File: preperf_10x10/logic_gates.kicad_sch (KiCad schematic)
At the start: 54 parts, among them J10 Conn_01x01_Pin, J11 Conn_01x01_Pin, J12 Conn_01x06_Pin, J13 Conn_01x02_Pin, J14 Conn_01x02_Pin, J15 Conn_01x02_Pin, J16 Conn_01x02_Pin, J17 Conn_01x01_Pin, J18 Conn_01x01_Pin, J19 Conn_01x01_Pin, J2 Conn_01x02_Pin, J20 Conn_01x01_Pin, J21 Conn_01x01_Pin, J22 Conn_01x01_Pin, J23 Conn_01x01_Pin, J24 Conn_01x01_Pin, J25 Conn_01x01_Pin, J26 Conn_01x01_Pin, J27 Conn_01x01_Pin, J28 Conn_01x01_Pin, J29 Conn_01x01_Pin, J3 Conn_01x02_Pin, J30 Conn_01x01_Pin, J31 Conn_01x01_Pin, J32 Conn_01x01_Pin, J33 Conn_01x02_Pin, J34 Conn_01x02_Pin, J35 Conn_01x02_Pin, J36 Conn_01x02_Pin, J5 Conn_01x02_Pin, J7 Conn_01x02_Pin, J8 Conn_01x01_Pin, J9 Conn_01x01_Pin, SW1 SW_DIP_x06, U1 74LS08, U3 74LS32, U4 74LS04, U5 74LS386

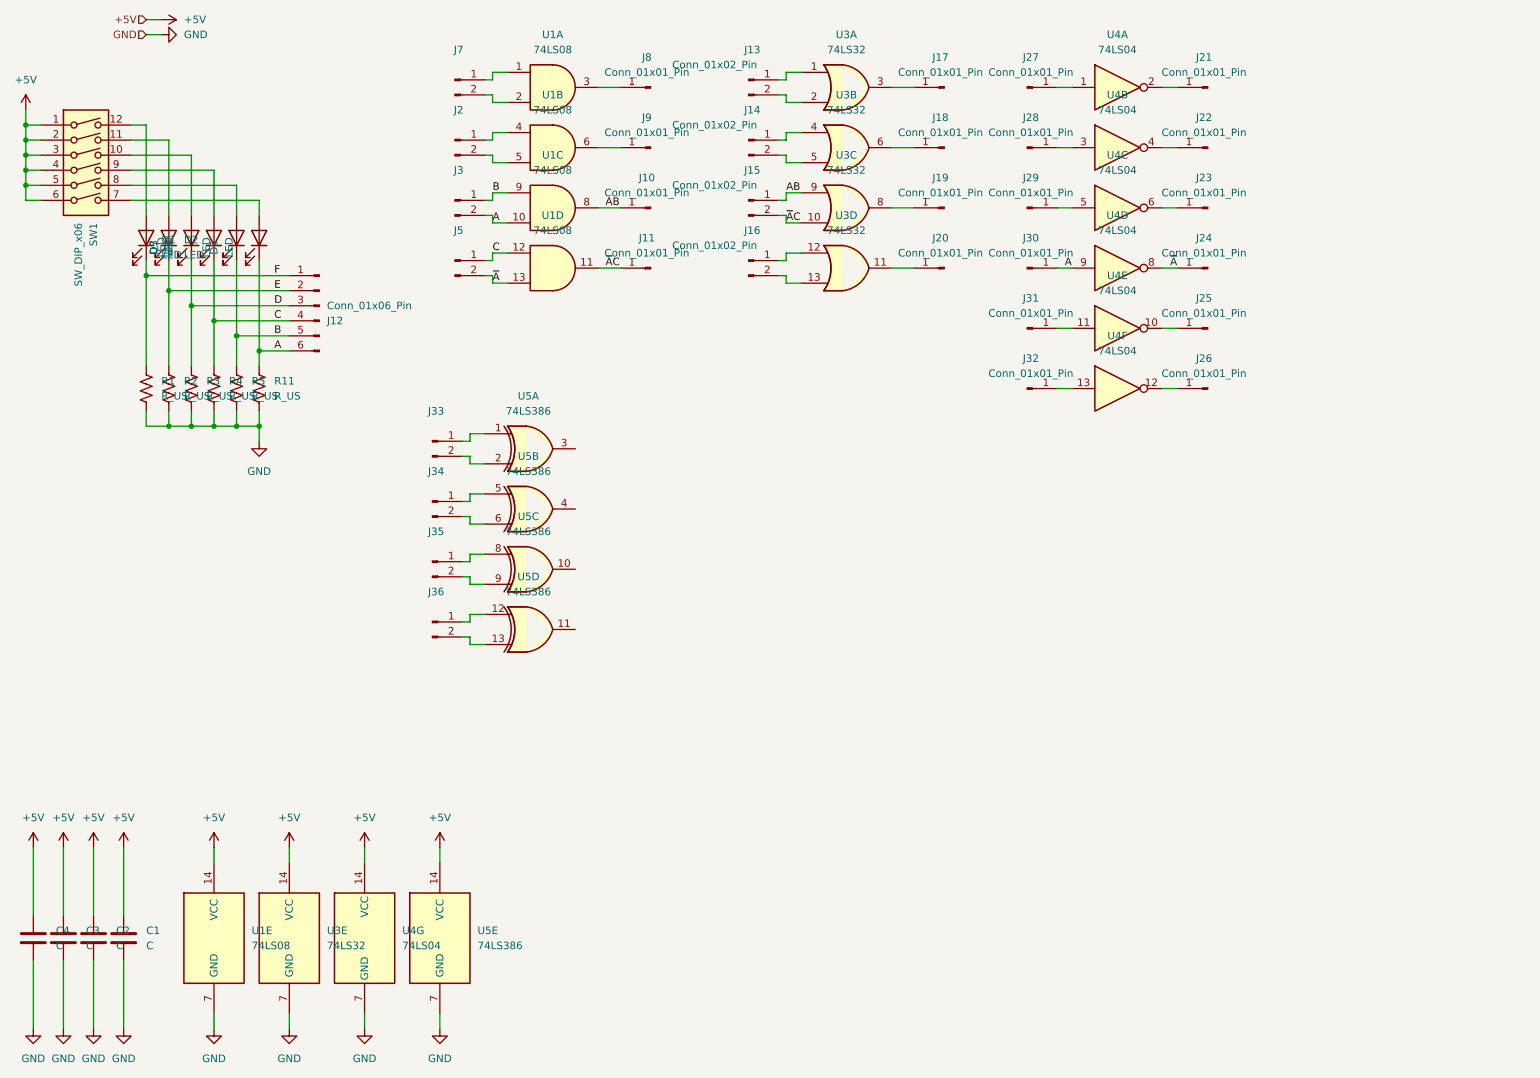
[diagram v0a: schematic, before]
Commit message: Added TP2, TP3 and TP4
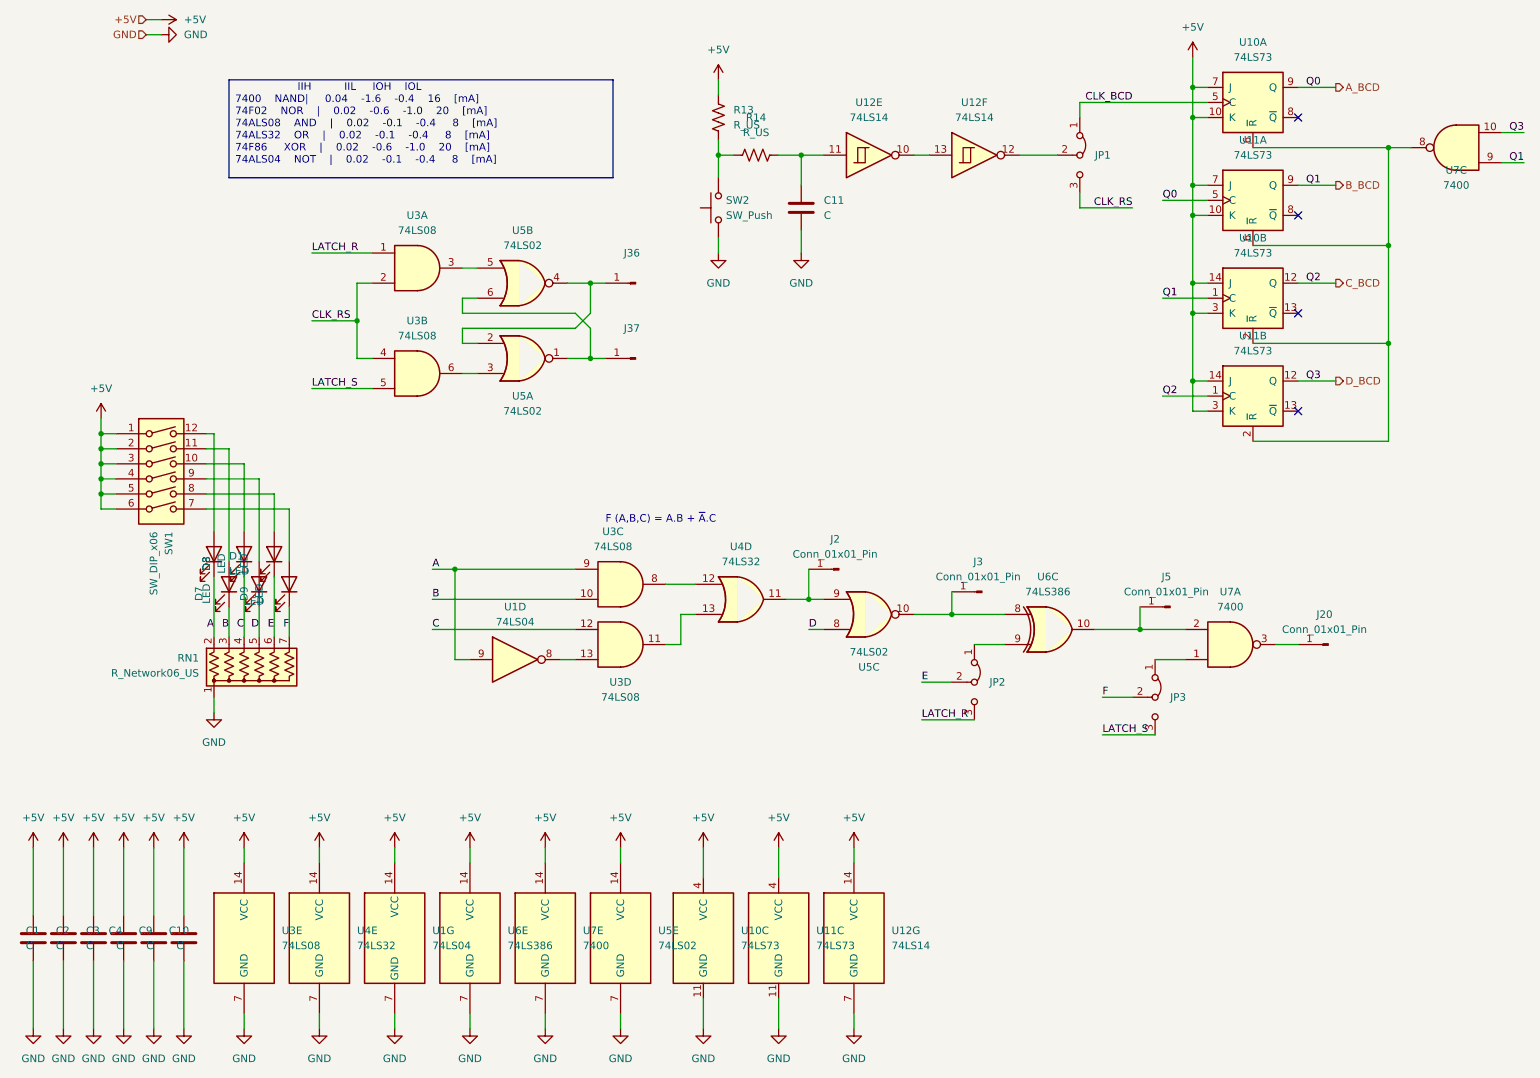
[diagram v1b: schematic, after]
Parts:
- removed J10, J11, J17, J18, J19, J21, J22, J23, J24, J25, J26, J27, J28, J29, J30, J31, J32, J8, J9: Conn_01x01_Pin, Connector_PinHeader_2.54mm:PinHeader_1x01_P2.54mm_Vertical, symbol Connector:Conn_01x01_Pin
- removed J12: Conn_01x06_Pin, Connector_PinHeader_2.54mm:PinHeader_1x06_P2.54mm_Vertical, symbol Connector:Conn_01x06_Pin
- removed J13, J14, J15, J16, J2, J3, J33, J34, J35, J36, J5, J7: Conn_01x02_Pin, Connector_PinHeader_2.54mm:PinHeader_1x02_P2.54mm_Vertical, symbol Connector:Conn_01x02_Pin
- removed R1, R11, R2, R3, R4, R5: R_US, Resistor_THT:R_Axial_DIN0207_L6.3mm_D2.5mm_P7.62mm_Horizontal, symbol Device:R_US
- removed unit 1 of U3
- removed unit 3 of U3
- removed unit 2 of U3
- removed unit 5 of U4
- removed unit 2 of U4
- removed unit 6 of U4
- removed unit 3 of U4
- removed unit 1 of U4
- removed unit 4 of U5
- removed unit 1 of U5
- removed unit 2 of U5
- added C10, C11, C9: C, Capacitor_THT:C_Disc_D5.0mm_W2.5mm_P2.50mm, symbol Device:C
- added J2, J3, J36, J37, J5: Conn_01x01_Pin, Connector_PinHeader_2.54mm:PinHeader_1x01_P2.54mm_Vertical, symbol Connector:Conn_01x01_Pin
- added JP1, JP2, JP3: Jumper_3_Bridged12, Connector_PinHeader_2.54mm:PinHeader_1x03_P2.54mm_Vertical, symbol Jumper:Jumper_3_Bridged12
- added R13: R_US, Resistor_THT:R_Axial_DIN0207_L6.3mm_D2.5mm_P7.62mm_Horizontal, symbol Device:R_US
- added R14: R_US, Resistor_THT:R_Axial_DIN0207_L6.3mm_D2.5mm_P2.54mm_Vertical, symbol Device:R_US
- added RN1: R_Network06_US, Resistor_THT:R_Array_SIP7, symbol Device:R_Network06_US
- added SW2: SW_Push, Button_Switch_THT:SW_PUSH_6mm_H7.3mm, symbol Switch:SW_Push
- added U10, U11: 74LS73, Package_DIP:DIP-14_W7.62mm_Socket, symbol 74xx:74LS73
- added U12: 74LS14, Package_DIP:DIP-14_W7.62mm_Socket, symbol 74xx:74LS14
- added U5: 74LS02, Package_DIP:DIP-14_W7.62mm_Socket, symbol 74xx:74LS02
- added U7: 7400, Package_DIP:DIP-14_W7.62mm_Socket, symbol 74xx:7400
- U6: renamed from U5; footprint (none) -> Package_DIP:DIP-14_W7.62mm_Socket
- renumbered C4 to C1, C3 to C2, C2 to C3, C1 to C4, U4 to U1, U1 to U3, U3 to U4
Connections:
- net AB is gone; now on an unnamed net: U3.8
- net ~{A}C is gone; now on an unnamed net: U3.11
- net +5V: now also C10.1, C9.1, R13.1, U10.10 (K), U10.14 (J), U10.3 (K), U10.4 (VCC), U10.7 (J), U11.10 (K), U11.14 (J), U11.3 (K), U11.4 (VCC), U11.7 (J), U12.14 (VCC), U5.14 (VCC), U7.14 (VCC)
- net A: now also D1.1 (K), U3.9, RN1.2 (R1); no longer D9.1 (K), U3.10
- net B: now also D2.1 (K), U3.10, RN1.3 (R2); no longer D8.1 (K), U3.9
- net C: now also D3.1 (K), RN1.4 (R3); no longer D7.1 (K)
- net D: now also D7.1 (K), RN1.5 (R4), U5.8; no longer D3.1 (K)
- net E: now also D8.1 (K), JP2.2 (C), RN1.6 (R5); no longer D2.1 (K)
- net F: now also D9.1 (K), JP3.2 (C), RN1.7 (R6); no longer D1.1 (K)
- net GND: now also C10.2, C11.2, C9.2, RN1.1 (common), SW2.1, U10.11 (GND), U11.11 (GND), U12.7 (GND), U5.7 (GND), U7.7 (GND)
- net at U6.10: now also J5.1 (Pin_1), U7.2
- net at U6.8: now also J3.1 (Pin_1), U5.10
- net at U6.9: now also JP2.1 (A)
- net LATCH_R: now reaches U3.1
- net LATCH_R: now also JP2.3 (B)
- net CLK_RS: now reaches U3.2
- net CLK_RS: now also U3.4, JP1.3 (B)
- net at U3.3: now also U5.5
- net at J20.1 (Pin_1): now also U7.3; no longer U4.11
- net LATCH_S: now reaches U3.5
- net LATCH_S: now also JP3.3 (B)
- net at U3.6: now also U5.3
- net ~{A}: no longer names the net of U1.8, U3.13
- new net: JP1.2 (C), U12.12
- new net: U12.10, U12.13
- new net: J2.1 (Pin_1), U4.11, U5.9
- new net: J37.1 (Pin_1), U5.1, U5.6
- new net: JP3.1 (A), U7.1
- new net: J36.1 (Pin_1), U5.2, U5.4
- new net: C11.1, R14.2, U12.11
- new net: U10.2 (~{R}), U10.6 (~{R}), U11.2 (~{R}), U11.6 (~{R}), U7.8
- new net: R13.2, R14.1, SW2.2
- new net A_BCD: U10.9 (Q), U11.5 (C)
- new net B_BCD: U10.1 (C), U11.9 (Q), U7.9
- new net CLK_BCD: JP1.1 (A), U10.5 (C)
- new net C_BCD: U10.12 (Q), U11.1 (C)
- new net D_BCD: U11.12 (Q), U7.10
- no-connect marks 0 -> 4
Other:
- note added: "F (A,B,C) = A.B + ~{A}.C"
- moved on the sheet: D1, D3, D7, D8, D9, SW1, U1D, U1G, U3A, U3B, U3C, U3D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

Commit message: "TP2" and "TP3" digital techniques
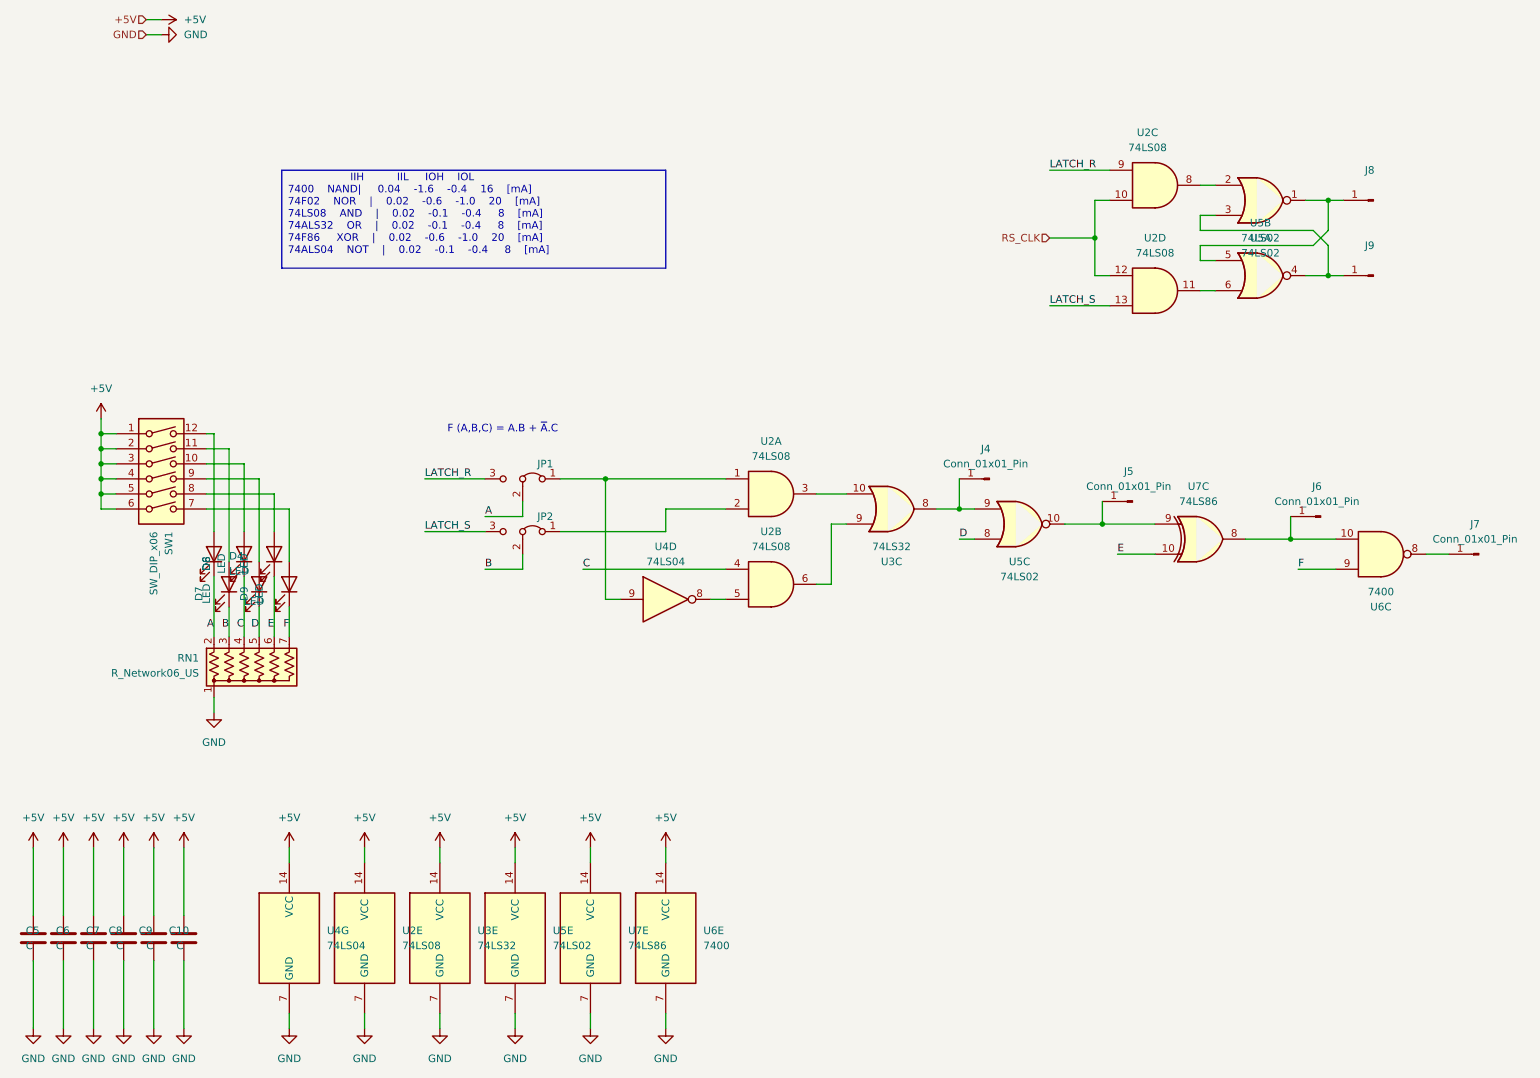
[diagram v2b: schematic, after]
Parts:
- removed C11: C, Capacitor_THT:C_Disc_D5.0mm_W2.5mm_P2.50mm, symbol Device:C
- removed J36, J37: Conn_01x01_Pin, Connector_PinHeader_2.54mm:PinHeader_1x01_P2.54mm_Vertical, symbol Connector:Conn_01x01_Pin
- removed JP3: Jumper_3_Bridged12, Connector_PinHeader_2.54mm:PinHeader_1x03_P2.54mm_Vertical, symbol Jumper:Jumper_3_Bridged12
- removed R13: R_US, Resistor_THT:R_Axial_DIN0207_L6.3mm_D2.5mm_P7.62mm_Horizontal, symbol Device:R_US
- removed R14: R_US, Resistor_THT:R_Axial_DIN0207_L6.3mm_D2.5mm_P2.54mm_Vertical, symbol Device:R_US
- removed SW2: SW_Push, Button_Switch_THT:SW_PUSH_6mm_H7.3mm, symbol Switch:SW_Push
- removed unit 7 of U1
- removed U10, U11: 74LS73, Package_DIP:DIP-14_W7.62mm_Socket, symbol 74xx:74LS73
- removed U12: 74LS14, Package_DIP:DIP-14_W7.62mm_Socket, symbol 74xx:74LS14
- removed unit 1 of U3
- removed unit 2 of U3
- removed unit 5 of U3
- removed U4: 74LS32, Package_DIP:DIP-14_W7.62mm_Socket, symbol 74xx:74LS32
- removed U6: 74LS386, Package_DIP:DIP-14_W7.62mm_Socket, symbol 74xx:74LS386
- removed U7: 7400, Package_DIP:DIP-14_W7.62mm_Socket, symbol 74xx:7400
- added J8, J9: Conn_01x01_Pin, Connector_PinHeader_2.54mm:PinHeader_1x01_P2.54mm_Vertical, symbol Connector:Conn_01x01_Pin
- added unit 5 of U2
- added unit 2 of U2
- added unit 1 of U2
- added U3: 74LS32, Package_DIP:DIP-14_W7.62mm_Socket, symbol 74xx:74LS32
- added unit 7 of U4
- added U6: 7400, Package_DIP:DIP-14_W7.62mm_Socket, symbol 74xx:7400
- added U7: 74LS86, Package_DIP:DIP-14_W7.62mm_Socket, symbol 74xx:74LS86
- C6: renamed from C2; footprint Capacitor_THT:C_Disc_D5.0mm_W2.5mm_P2.50mm -> Capacitor_THT:C_Disc_D5.0mm_W2.5mm_P5.00mm
- C7: renamed from C3; footprint Capacitor_THT:C_Disc_D5.0mm_W2.5mm_P2.50mm -> Capacitor_THT:C_Disc_D5.0mm_W2.5mm_P5.00mm
- D9: footprint LED_THT:LED_D3.0mm_FlatTop -> LED_THT:LED_D3.0mm
- renumbered C1 to C5, C4 to C8, D1 to D4, D2 to D5, D3 to D6, J2 to J4, J3 to J5, J5 to J6, J20 to J7, U3 to U2, U1 to U4
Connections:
- net CLK_RS is gone; now on net LATCH_R: JP1.3 (B)
- net +5V: now also U2.14 (VCC), U3.14 (VCC), U4.14 (VCC), U6.14 (VCC), U7.14 (VCC)
- net A: now also JP1.2 (C); no longer U2.9, U4.9
- net B: now also JP2.2 (C); no longer U2.10
- net C: now also U2.4; no longer U2.12
- net E: now also U7.10; no longer JP2.2 (C)
- net F: now also U6.9
- net GND: now also U2.7 (GND), U3.7 (GND), U4.7 (GND), U6.7 (GND), U7.7 (GND)
- net LATCH_R: now also U2.9; no longer JP2.3 (B)
- net LATCH_S: now also JP2.3 (B), U2.13
- net at U2.11: now also U5.6
- net at U4.8: now also U2.5; no longer U2.13
- net at J7.1 (Pin_1): now also U6.8
- net at J6.1 (Pin_1): now also U6.10, U7.8
- net at J5.1 (Pin_1), U5.10: now also U7.9
- net at JP2.1 (A): now also U2.2
- net at U5.5: now also U5.1, J8.1 (Pin_1)
- net at J4.1 (Pin_1), U5.9: now also U3.8
- net at U2.8: now also U5.2
- net at U5.4: now also U5.3, J9.1 (Pin_1); no longer U5.2
- net CLK_BCD: no longer names the net of JP1.1 (A)
- net CLK_BCD: now also U4.9, U2.1
- new net: U2.6, U3.9
- new net: U2.3, U3.10
- new net RS_CLK: U2.10, U2.12
- no-connect marks 4 -> 0
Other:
- moved on the sheet: J4, J5, J6, J7, U2C, U2D, U4D, U5C

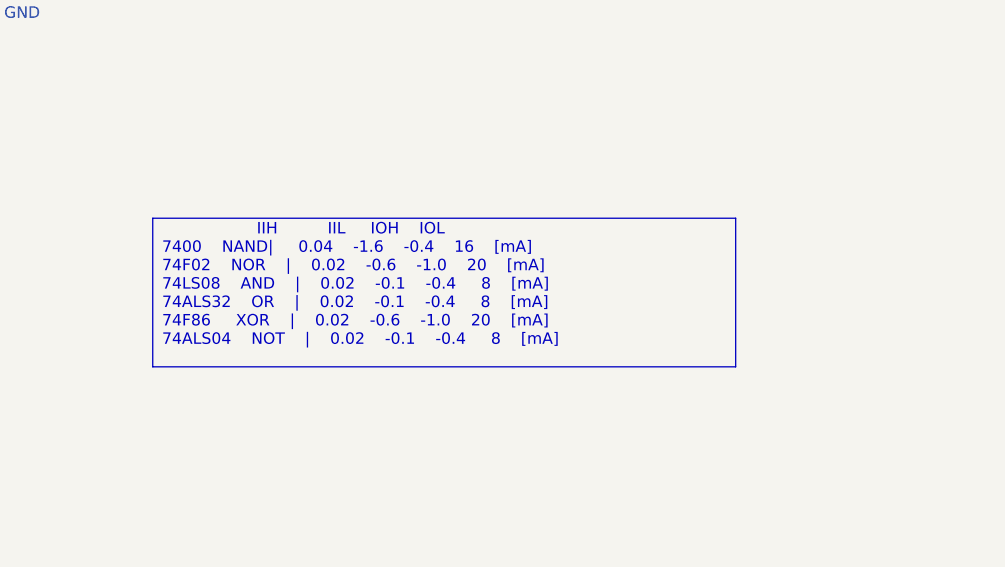
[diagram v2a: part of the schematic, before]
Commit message: Update. Delete TP4
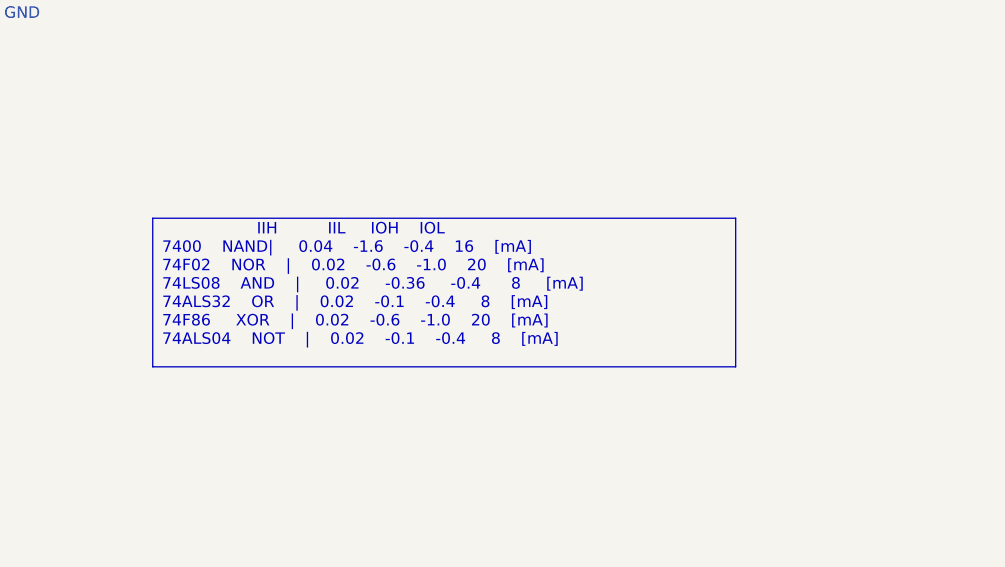
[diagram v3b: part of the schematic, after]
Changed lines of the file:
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@@
     (stroke (width 0) (type default))
   )
-  (text_box "	 		  	IIH	 	 IIL	 IOH	IOL\n7400	NAND| 	0.04	-1.6	-0.4	16	[mA]\n74F02	NOR	|	0.02	-0.6	-1.0	20	[mA]\n74LS08	AND	|	0.02	-0.1	-0.4	 8	[mA]\n74ALS32	OR	|	0.02	-0.1	-0.4	 8	[mA]\n74F86 	XOR	|	0.02	-0.6	-1.0	20	[mA]\n74ALS04	NOT	|	0.02	-0.1	-0.4	 8	[mA]\n\n"
+  (text_box "	 		  	IIH	 	 IIL	 IOH	IOL\n7400	NAND| 	0.04	-1.6	-0.4	16	[mA]\n74F02	NOR	|	0.02	-0.6	-1.0	20	[mA]\n74LS08	AND	| 	0.02 	-0.36 	-0.4 	 8 	[mA]\n74ALS32	OR	|	0.02	-0.1	-0.4	 8	[mA]\n74F86 	XOR	|	0.02	-0.6	-1.0	20	[mA]\n74ALS04	NOT	|	0.02	-0.1	-0.4	 8	[mA]\n\n"
     (at 69.85 40.64 0) (size 64.77 16.51)
     (stroke (width 0) (type solid) (color 0 0 0 1))
